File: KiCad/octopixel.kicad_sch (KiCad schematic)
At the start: 8 parts, among them J2 RBG PB3, J3 RBG PB4, J4 RBG PB5, J5 RBG_PB3, J6 Octopus SPI3, U1 CD4050BE

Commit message: Intial commit for SMD version
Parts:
- removed H1, H2: MountingHole, MountingHole:MountingHole_3.2mm_M3_DIN965_Pad, symbol Mechanical:MountingHole
- removed J2: RBG PB3, Connector_JST:JST_XH_B3B-XH-AM_1x03_P2.50mm_Vertical, symbol Connector_Generic:Conn_01x03
- removed J3: RBG PB4, Connector_JST:JST_XH_B3B-XH-AM_1x03_P2.50mm_Vertical, symbol Connector_Generic:Conn_01x03
- removed J4: RBG PB5, Connector_JST:JST_XH_B3B-XH-AM_1x03_P2.50mm_Vertical, symbol Connector_Generic:Conn_01x03
- removed J5: RBG_PB3, Connector_JST:JST_XH_B3B-XH-AM_1x03_P2.50mm_Vertical, symbol Connector_Generic:Conn_01x03
- removed U1: CD4050BE, easyeda:DIP-16_L20.3-W10.2-P2.54-LS10.2-BL, symbol easyeda:CD4050BE
- added CN5, CN6, CN7, CN8: PH2.0-3PWB Horizontal, easyeda:CONN-TH_PH-3PWB, symbol easyeda:PH2.0-3PWBHorizontal
- added U2: TXS0104EPWR, easyeda:TSSOP-14_L5.0-W4.4-P0.65-LS6.4-BL, symbol easyeda:TXS0104EPWR
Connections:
- net +3V3: now also U2.1 (VCCA), U2.8 (OE)
- net +5V: now also CN5.1, CN6.1, CN7.1, CN8.1, U2.14 (VCCB)
- net GND: now also U2.7 (GND)
- net PA15: now also U2.5 (A4)
- net PA15_{5V}: now also CN5.2, U2.10 (B4)
- net PB3: now also U2.2 (A1)
- net PB3_{5V}: now also CN6.2, U2.13 (B1)
- net PB4: now also U2.3 (A2)
- net PB4_{5V}: now also CN7.2, U2.12 (B2)
- net PB5: now also U2.4 (A3)
- net PB5_{5V}: now also CN8.2, U2.11 (B3)
- no-connect marks 6 -> 10

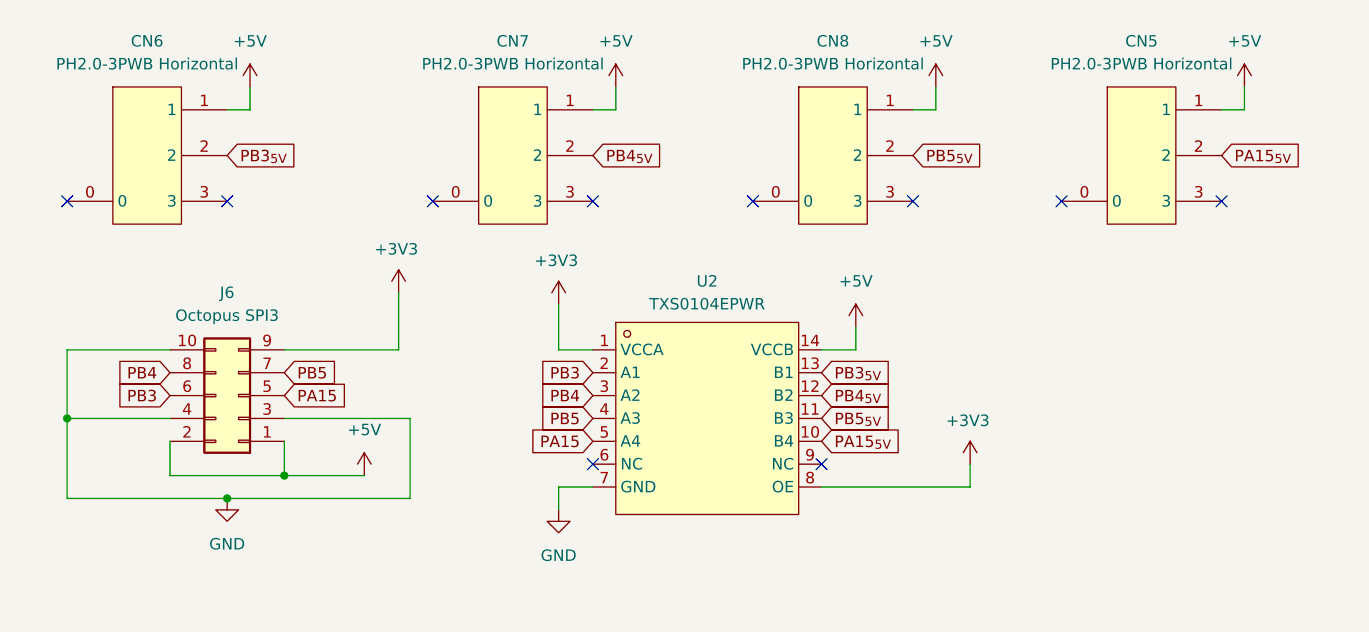
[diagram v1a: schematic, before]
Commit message: Included missing grounds for connectors
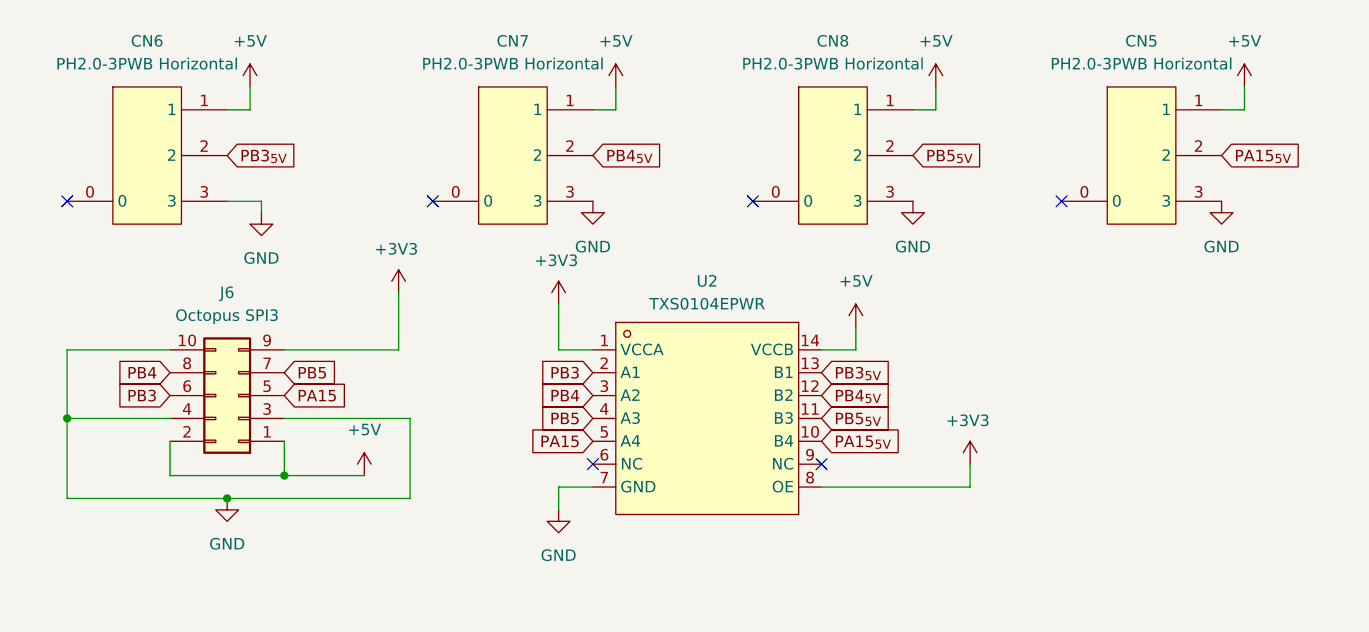
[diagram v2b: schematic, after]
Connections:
- net GND: now also CN5.3, CN6.3, CN7.3, CN8.3
- no-connect marks 10 -> 6
